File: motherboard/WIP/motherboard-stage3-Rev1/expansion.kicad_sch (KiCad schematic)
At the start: 10 parts, among them P1 VideoAddon, P2 AudioAddon, P3 ExpansionPort, P4 Compact Flash Addon

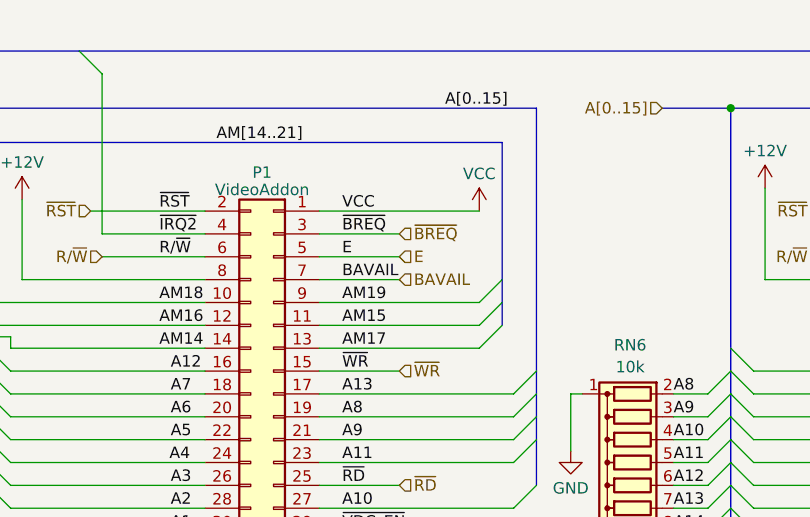
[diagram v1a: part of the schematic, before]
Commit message: Added Support for protected mode, routed R/W thru logic to amplify.
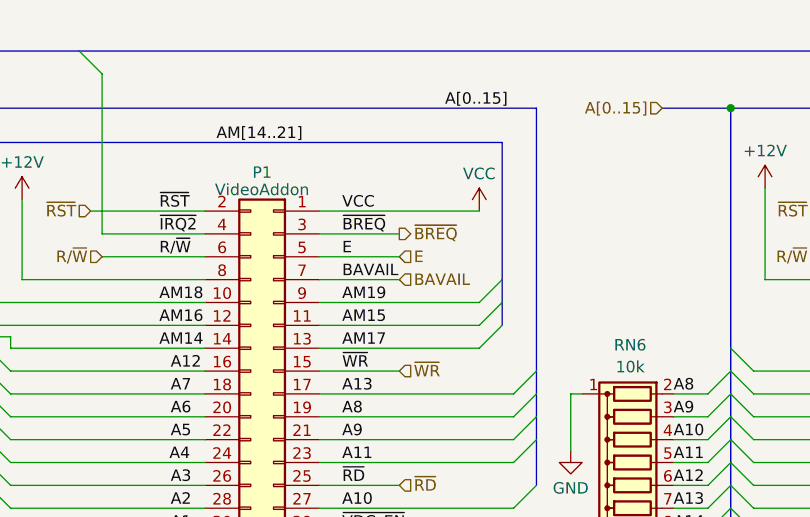
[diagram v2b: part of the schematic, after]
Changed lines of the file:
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@@
 	)
 	(hierarchical_label "~{BREQ}"
-		(shape input)
+		(shape output)
 		(at 86.36 58.42 0)
 		(effects
